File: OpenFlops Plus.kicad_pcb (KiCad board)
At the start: 2 copper layers, 111.6 x 59.4 mm, 80 parts, among them J1 Conn_02x05_Odd_Even, J2 Conn_02x05_Odd_Even, J3 Conn_01x04, P1 Conn_02x17_Odd_Even, P2 171826-4, P3 Conn_01x04, P4 Micro_SD_Card_Det1, P5 Conn_01x04, P6 Conn_01x05, Q1 BSS138, Q2 BSS138, Q3 BSS138, Q4 BSS138, Q5 BSS138, Q6 BSS138, Q7 SS8050, SW1 BT_RIGHT, SW2 BT_LEFT, U1 AMS1117-3.3, U2 STM32F105RBT6, U3 74HCT04, U4 CH213K, U5 SRV05-4, Y1 8MHz

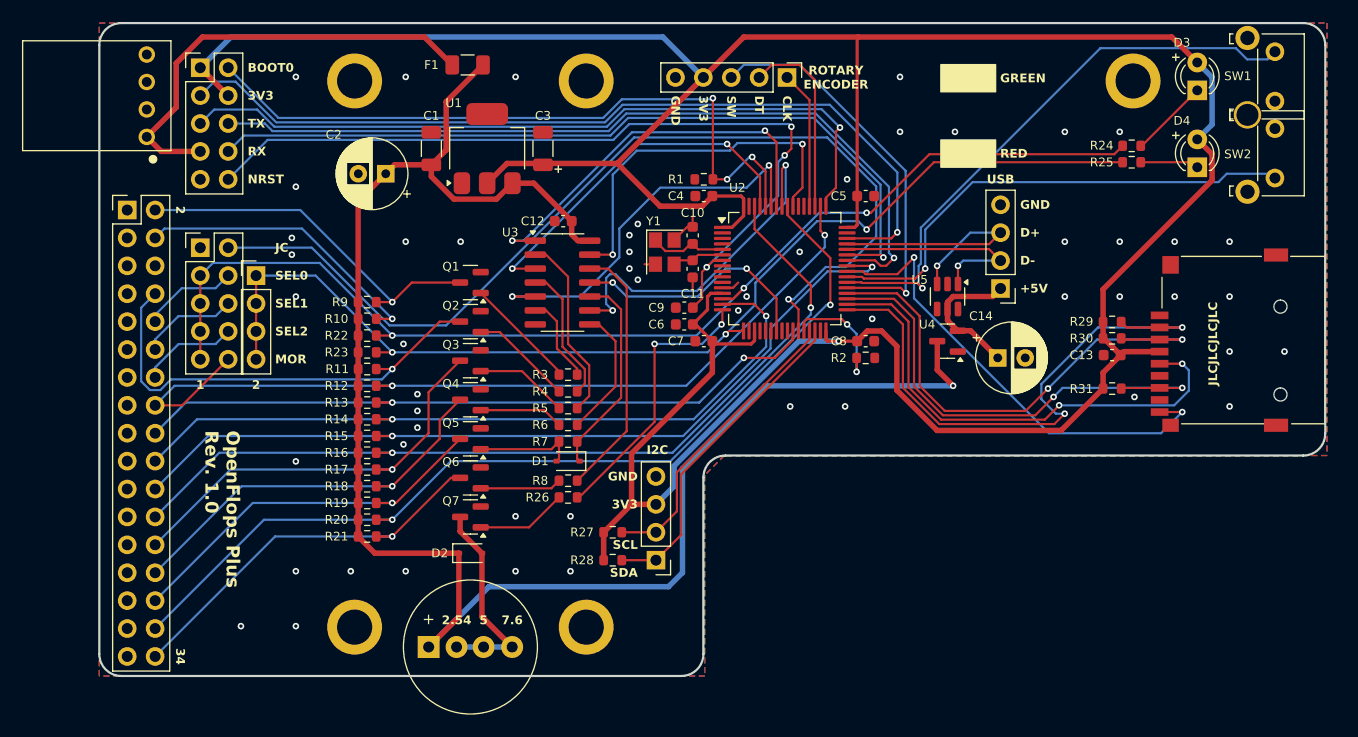
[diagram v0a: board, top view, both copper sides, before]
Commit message: Add PMOS for card reader
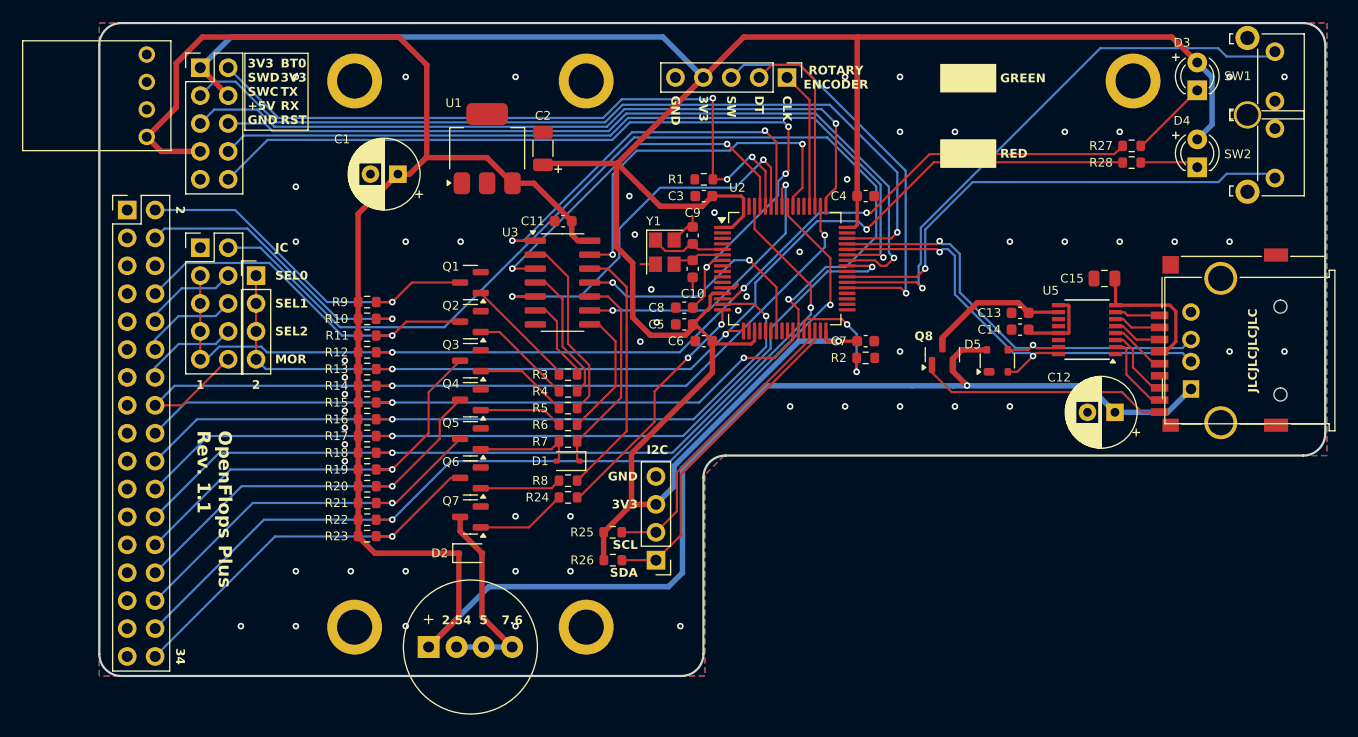
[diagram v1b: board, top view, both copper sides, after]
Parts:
- removed the C1 at (122.9, 86.7)
- removed F1: Polyfuse, Fuse:Fuse_1206_3216Metric
- removed R29, R30, R31: 47K, Resistor_SMD:R_0603_1608Metric
- removed U4: CH213K, Package_TO_SOT_SMD:SOT-23
- added C14: 4.7uF, Capacitor_SMD:C_0603_1608Metric, F.Cu at (176.5, 103.2)
- added C15: 10uF, Capacitor_SMD:C_0805_2012Metric, F.Cu at (184.2, 98.5)
- added D5: SR05, Package_TO_SOT_SMD:SOT-143, F.Cu at (174.4, 106.0)
- added Q8: AO3401A, Package_TO_SOT_SMD:SOT-23, F.Cu at (169.4, 105.5)
- C12: renamed from C13; value 10uF -> 100uF; footprint Capacitor_SMD:C_0603_1608Metric -> Capacitor_THT:CP_Radial_D6.3mm_P2.50mm
- C13: renamed from C14; value 100uF -> 1uF; footprint Capacitor_THT:CP_Radial_D6.3mm_P2.50mm -> Capacitor_SMD:C_0603_1608Metric
- P3: value Conn_01x04 -> USB_A; footprint Connector_PinHeader_2.54mm:PinHeader_1x04_P2.54mm_Vertical -> Connector_USB:USB_A_Molex_67643_Horizontal
- R25, R26: value 1K -> 4.7K
- R27, R28: value 4.7K -> 1K
- U5: value SRV05-4 -> GL823K; footprint Package_TO_SOT_SMD:SOT-23-6 -> Package_SO:SSOP-16_3.9x4.9mm_P0.635mm
- moved R24 60.5 mm to (135.4, 118.5), turned to 180 degrees
- moved R28 59.5 mm to (186.7, 88.0), turned to 0 degrees
- moved R27 58.9 mm to (186.7, 86.5), turned to 0 degrees
- moved R25 58.0 mm to (139.4, 121.6), turned to 180 degrees
- moved P3 19.6 mm to (192.1, 108.6), turned to 90 degrees
- moved R22 16.8 mm to (117.1, 120.5), turned to 0 degrees
- moved R23 16.7 mm to (117.1, 122.0), turned to 0 degrees
- moved U5 13.1 mm to (182.6, 103.2), turned to 180 degrees
- moved R26 7.02 mm to (139.4, 124.2)
- moved C12 5.21 mm to (185.2, 110.7), turned to 180 degrees
- moved C13 4.57 mm to (176.5, 101.7)
- moved R11 3.05 mm to (117.1, 103.7)
- moved R12 3.05 mm to (117.1, 105.3), turned to 180 degrees
- moved R15 3.05 mm to (117.1, 109.8)
- moved R16 3.05 mm to (117.1, 111.3)
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- renumbered C2 to C1, C11 to C10, C12 to C11, C3 to C2, C4 to C3, C5 to C4, C6 to C5, C7 to C6, C8 to C7, C9 to C8, C10 to C9
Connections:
- C12 pad 1: GND -> +5V
- C12 pad 2: +3V3 -> GND
- C13 pad 1: Net-(P3-Pin_1) -> GND
- C13 pad 2: GND -> Net-(Q8-D)
- J1 pad 7: /VBUS -> +5V
- P2 pad 1: /VBUS -> +5V
- P3 pad 1: Net-(P3-Pin_1) -> +5V
- P4 pad 1: unconnected-(P4-DAT2-Pad1) -> Net-(P4-DAT2)
- P4 pad 11: (no net) -> GND
- P4 pad 12: (no net) -> GND
- P4 pad 13: (no net) -> GND
- P4 pad 2: /SPI_NSS -> Net-(P4-DAT3/CD)
- P4 pad 3: /SPI_MOSI -> Net-(P4-CMD)
- P4 pad 4: +3V3 -> Net-(P4-VDD)
- P4 pad 5: /SPI_SCLK -> Net-(P4-CLK)
- P4 pad 7: /SPI_MISO -> Net-(P4-DAT0)
- P4 pad 8: unconnected-(P4-DAT1-Pad8) -> Net-(P4-DAT1)
- P4 pad 9: /~{SD_CD} -> /SD_DET
- R12 pad 1: +5V -> /~{SELX}
- R12 pad 2: /~{MTRON} -> +5V
- R13 pad 1: +5V -> /~{SELY}
- R13 pad 2: /~{DIR} -> +5V
- R14 pad 2: /~{STEP} -> /~{MTRON}
- R15 pad 2: /~{WDATA} -> /~{DIR}
- R16 pad 2: /~{WGATE} -> /~{STEP}
- R17 pad 2: /~{TRK0} -> /~{WDATA}
- R18 pad 2: /~{WPROT} -> /~{WGATE}
- R19 pad 2: /~{RDATA} -> /~{TRK0}
- R20 pad 2: /~{SIDE} -> /~{WPROT}
- R21 pad 2: /~{RDY} -> /~{RDATA}
- R22 pad 1: /~{SELX} -> +5V
- R22 pad 2: +5V -> /~{SIDE}
- R23 pad 1: /~{SELY} -> +5V
- R23 pad 2: +5V -> /~{RDY}
- R24 pad 1: /~{SELX} -> /SPK
- R24 pad 2: Net-(D3-K) -> Net-(Q7-B)
- R25 pad 1: /~{SELY} -> /I2C_SCL
- R25 pad 2: Net-(D4-K) -> +3V3
- R26 pad 1: /SPK -> /I2C_SDA
- R26 pad 2: Net-(Q7-B) -> +3V3
- R27 pad 1: /I2C_SCL -> /~{SELX}
- R27 pad 2: +3V3 -> Net-(D3-K)
- R28 pad 1: /I2C_SDA -> /~{SELY}
- R28 pad 2: +3V3 -> Net-(D4-K)
- U2 pad 53: unconnected-(U2-PC12-Pad53) -> GND
- U5 pad 1: /USB_D- -> GND
- U5 pad 2: GND -> Net-(P4-DAT1)
- U5 pad 3: /USB_D+ -> Net-(P4-DAT0)
- U5 pad 4: unconnected-(U5-IO3-Pad4) -> Net-(P4-CLK)
- U5 pad 5: Net-(P3-Pin_1) -> Net-(P4-CMD)
- U5 pad 6: unconnected-(U5-IO4-Pad6) -> Net-(P4-DAT3/CD)
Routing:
- net +5V: track 156.7 -> 215.5 mm
- net /SPI_NSS: track 52.7 -> 0.00 mm, vias 2 -> 0
- net +3V3: track 295.5 -> 248.2 mm
- net /SPI_MOSI: track 47.0 -> 0.00 mm, vias 2 -> 0
- net /SPI_MISO: track 45.4 -> 0.00 mm, vias 2 -> 0
- net /SPI_SCLK: track 44.8 -> 0.00 mm, vias 2 -> 0
- net /~{SD_CD}: track 42.9 -> 0.00 mm, vias 2 -> 0
- net /VBUS: track 40.4 -> 0.00 mm
- net /USB_D-: track 20.1 -> 43.4 mm, vias 1 -> 2
- net /SD_DET: track 0.00 -> 22.9 mm
- net /USB_D+: track 23.1 -> 43.1 mm, vias 1 -> 2
- net Net-(P3-Pin_1): track 13.0 -> 0.00 mm
- net Net-(Q8-D): track 0.00 -> 12.9 mm
- net Net-(P4-VDD): track 0.00 -> 12.8 mm
- net /~{INDEX}: track 42.4 -> 34.2 mm
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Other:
- board text added: "3V3 SWD SWC +5V GND"
- board text added: "BT0 3V3 TX RX RST"
- board text added: "OpenFlops Plus Rev. 1.1"
- board text removed: "+5V"
- board text removed: "BOOT0"
- board text removed: "D+"
- board text removed: "D-"
- board text removed: "NRST"
- board text removed: "OpenFlops Plus Rev. 1.0"
- board text removed: "RX"
- board text removed: "TX"
- board text removed: "USB"

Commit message: Move to 74LS07
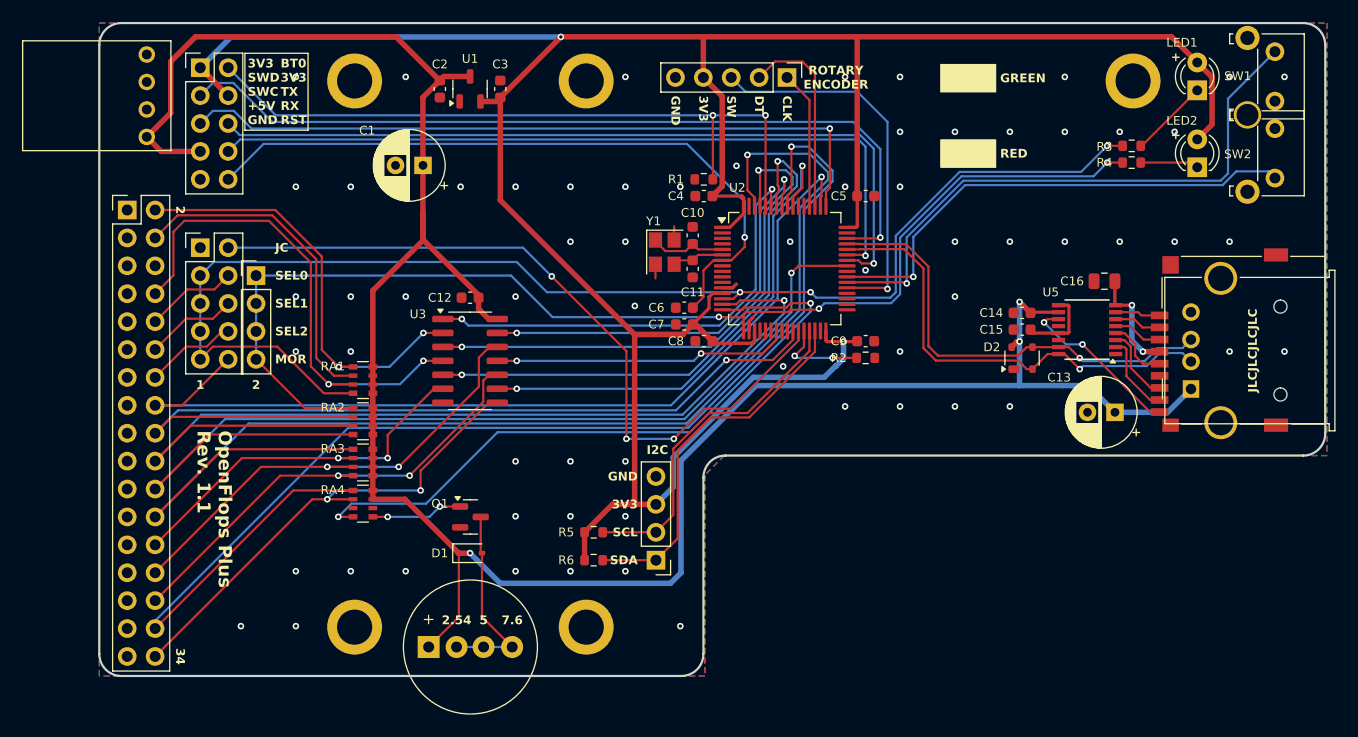
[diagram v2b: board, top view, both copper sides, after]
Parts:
- removed the C11 at (134.9, 93.3)
- removed the D1 at (135.4, 115.2)
- removed D5: SR05, Package_TO_SOT_SMD:SOT-143
- removed the Q1 at (126.5, 98.9)
- removed Q2, Q3, Q4, Q5, Q6: BSS138, Package_TO_SOT_SMD:SOT-23
- removed Q8: AO3401A, Package_TO_SOT_SMD:SOT-23
- removed R10, R11, R12, R13, R14, R15, R16, R17, R18, R19, R20, R21, R22, R23, R24, R7, R8, R9: 1K, Resistor_SMD:R_0603_1608Metric
- removed the R3 at (135.4, 107.3)
- removed the R4 at (135.4, 108.8)
- removed the R5 at (135.4, 110.3)
- removed the R6 at (135.4, 111.9)
- added C12: 100nF, Capacitor_SMD:C_0603_1608Metric, F.Cu at (126.5, 100.3)
- added C3: 1uF, Capacitor_SMD:C_0603_1608Metric, F.Cu at (129.2, 81.3)
- added D2: SR05, Package_TO_SOT_SMD:SOT-143, F.Cu at (176.7, 105.8)
- added RA1: 1K, Resistor_SMD:R_Array_Convex_4x0603, F.Cu at (116.7, 107.8)
- added RA2: 1K, Resistor_SMD:R_Array_Convex_4x0603, F.Cu at (116.7, 111.5)
- added RA3: 1K, Resistor_SMD:R_Array_Convex_4x0603, F.Cu at (116.7, 115.3)
- added RA4: 1K, Resistor_SMD:R_Array_Convex_4x0603, F.Cu at (116.7, 119.0)
- C2: value 22uF -> 1uF; footprint Capacitor_SMD:C_1206_3216Metric -> Capacitor_SMD:C_0603_1608Metric
- U1: value AMS1117-3.3 -> XC6206P332MR-G; footprint Package_TO_SOT_SMD:SOT-223-3_TabPin2 -> Package_TO_SOT_SMD:SOT-23-3
- U3: value 74HCT04 -> 74LS07
- moved U3 11.0 mm to (126.5, 106.0)
- moved C2 10.8 mm to (123.7, 81.3), turned to -90 degrees
- moved U1 5.65 mm to (126.5, 81.3)
- moved C1 2.42 mm to (122.2, 88.2)
- moved R6 1.75 mm to (137.7, 124.2)
- moved R5 1.74 mm to (137.7, 121.6)
- moved C16 0.25 mm to (184.2, 98.8)
- moved C14 0.18 mm to (176.7, 101.7)
- moved C15 0.18 mm to (176.7, 103.2)
- turned Q1 to 0 degrees
- renumbered C9 to C10, C10 to C11, C12 to C13, C13 to C14, C14 to C15, C15 to C16, C3 to C4, C4 to C5, C8 to C6, C5 to C7, C6 to C8, C7 to C9, D2 to D1, D3 to LED1, D4 to LED2, Q7 to Q1, R27 to R3, R28 to R4, R25 to R5, R26 to R6, LS1 to SPK1
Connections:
- C14 pad 2: Net-(Q8-D) -> +5V
- C2 pad 1: +3V3 -> +5V
- P4 pad 9: /SD_DET -> Net-(P4-DET)
- U3 pad 1: /~{TRK0_3V3} -> /~{DSKCHG_3V3}
- U3 pad 10: Net-(D1-K) -> /~{RDATA}
- U3 pad 12: Net-(R8-Pad1) -> /~{WPROT}
- U3 pad 13: /~{RDY_3V3} -> /~{WPROT_3V3}
- U3 pad 2: Net-(R5-Pad1) -> /~{DSKCHG}
- U3 pad 4: Net-(R4-Pad1) -> /~{INDEX}
- U3 pad 5: /~{DSKCHG_3V3} -> /~{TRK0_3V3}
- U3 pad 6: Net-(R3-Pad1) -> /~{TRK0}
- U3 pad 8: Net-(R6-Pad1) -> /~{RDY}
- U3 pad 9: /~{WPROT_3V3} -> /~{RDY_3V3}
- U5 pad 10: Net-(Q8-D) -> +5V
- U5 pad 11: unconnected-(U5-GPIO-Pad11) -> Net-(P4-DET)
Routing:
- net /SPK: track 22.7 -> 61.1 mm
- net /~{SIDE}: track 85.7 -> 118.8 mm, vias 2 -> 1
- net /~{WGATE}: track 80.8 -> 113.7 mm, vias 2 -> 1
- net Net-(R8-Pad1): track 23.5 -> 0.00 mm
- net /SD_DET: track 22.9 -> 0.00 mm
- net /JC: track 89.2 -> 68.4 mm, vias 1 -> 3
- net /~{STEP}: track 68.7 -> 89.1 mm, vias 2 -> 1
- net Net-(D1-K): track 18.9 -> 0.00 mm
- net /~{DIR}: track 63.9 -> 81.0 mm, vias 2 -> 1
- net Net-(R5-Pad1): track 17.0 -> 0.00 mm
- net /~{INDEX_3V3}: track 33.3 -> 49.6 mm
- net /~{SELX}: track 103.9 -> 120.2 mm
- net Net-(P4-DET): track 0.00 -> 15.3 mm, vias 0 -> 2
- net /~{WDATA}: track 78.5 -> 93.6 mm, vias 2 -> 1
- net /~{TRK0_3V3}: track 36.6 -> 51.1 mm
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
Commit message: Use SPI to manipulate SD card
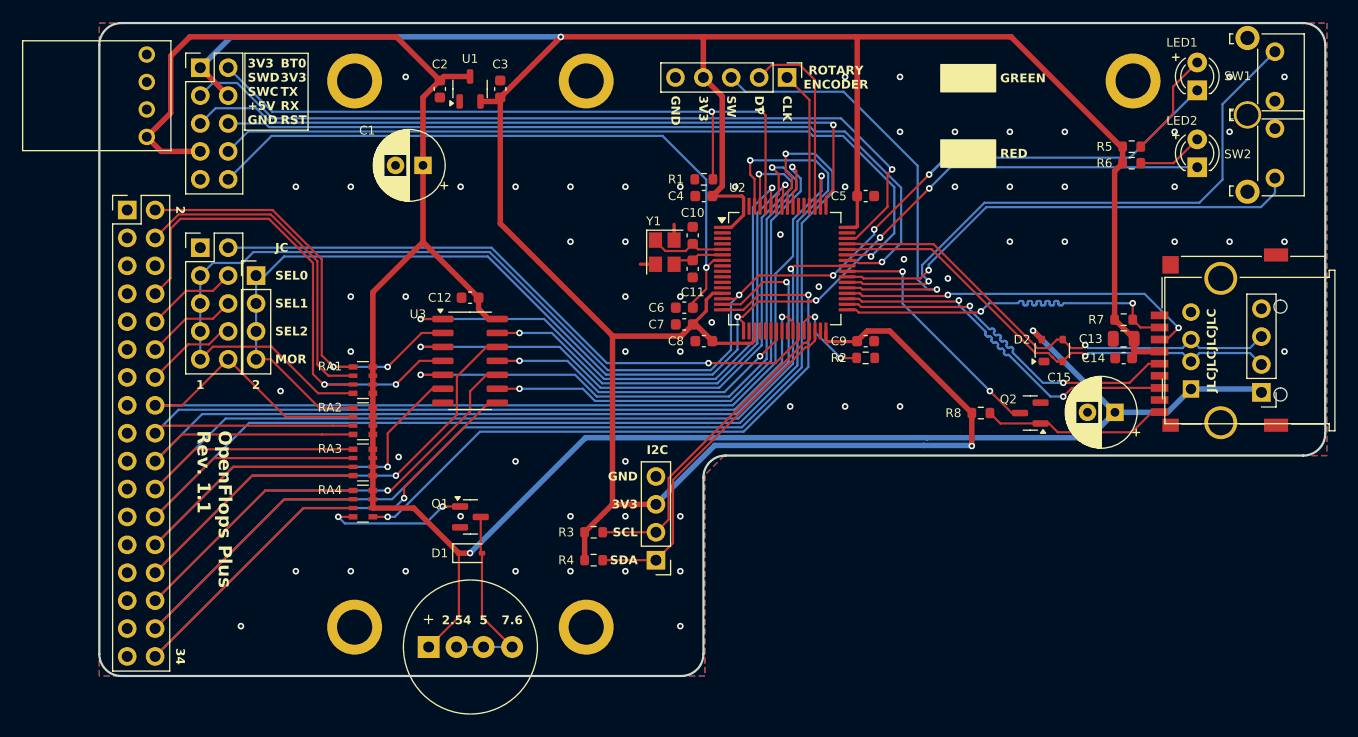
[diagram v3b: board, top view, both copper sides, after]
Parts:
- removed the C15 at (176.7, 103.2)
- removed C16: 10uF, Capacitor_SMD:C_0805_2012Metric
- removed U5: GL823K, Package_SO:SSOP-16_3.9x4.9mm_P0.635mm
- added C13: 10uF, Capacitor_SMD:C_0805_2012Metric, F.Cu at (185.9, 104.0)
- added J4: Conn_01x04, Connector_PinHeader_2.54mm:PinHeader_1x04_P2.54mm_Vertical, F.Cu at (198.5, 108.9)
- added Q2: BSS138, Package_TO_SOT_SMD:SOT-23, F.Cu at (177.4, 110.8)
- added R7: 47K, Resistor_SMD:R_0603_1608Metric, F.Cu at (185.9, 102.3)
- added R8: 10K, Resistor_SMD:R_0603_1608Metric, F.Cu at (172.9, 110.8)
- C14: value 1uF -> 100nF
- U1: value XC6206P332MR-G -> ME6211A33M3G-N
- moved C14 10.1 mm to (185.9, 105.8), turned to 180 degrees
- moved D2 2.83 mm to (179.4, 105.1)
- moved R5 0.07 mm to (186.7, 86.5), turned to 180 degrees
- turned R6 to 180 degrees
- renumbered C13 to C15, R5 to R3, R6 to R4, R3 to R5, R4 to R6
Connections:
- C14 pad 1: GND -> +3V3
- C14 pad 2: +5V -> GND
- LED1 pad 1: Net-(LED1-K) -> /~{SELX}
- LED1 pad 2: +3V3 -> Net-(LED1-A)
- LED2 pad 1: Net-(LED2-K) -> /~{SELY}
- LED2 pad 2: +3V3 -> Net-(LED2-A)
- P4 pad 1: Net-(P4-DAT2) -> unconnected-(P4-DAT2-Pad1)
- P4 pad 2: Net-(P4-DAT3/CD) -> /SPI_NSS
- P4 pad 3: Net-(P4-CMD) -> /SPI_MOSI
- P4 pad 4: Net-(P4-VDD) -> +3V3
- P4 pad 5: Net-(P4-CLK) -> /SPI_SCLK
- P4 pad 7: Net-(P4-DAT0) -> /SPI_MISO
- P4 pad 8: Net-(P4-DAT1) -> unconnected-(P4-DAT1-Pad8)
- P4 pad 9: Net-(P4-DET) -> /~{SD_CD}
- R5 pad 1: /~{SELX} -> Net-(LED1-A)
- R5 pad 2: Net-(LED1-K) -> +3V3
- R6 pad 1: /~{SELY} -> Net-(LED2-A)
- R6 pad 2: Net-(LED2-K) -> +3V3
- RA2 pad 2: /~{DIR} -> /~{MTRON}
- RA2 pad 3: /~{STEP} -> /~{DIR}
- RA2 pad 4: /~{WDATA} -> /~{STEP}
- RA3 pad 1: /~{WGATE} -> /~{WDATA}
- RA3 pad 2: /~{TRK0} -> /~{WGATE}
- RA3 pad 3: /~{WPROT} -> /~{TRK0}
- RA3 pad 4: /~{RDATA} -> /~{WPROT}
- RA4 pad 1: /~{SIDE} -> /~{RDATA}
- RA4 pad 2: /~{RDY} -> /~{SIDE}
- RA4 pad 3: (no net) -> /~{RDY}
- RA4 pad 4: /SPK -> Net-(Q1-B)
- RA4 pad 5: Net-(Q1-B) -> /SPK
- RA4 pad 6: (no net) -> +5V
- U2 pad 40: /~{SD_CD} -> /SD_CD
- U2 pad 53: GND -> unconnected-(U2-PC12-Pad53)
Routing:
- net +3V3: track 254.1 -> 288.7 mm
- net /SPI_MOSI: track 0.00 -> 33.8 mm, vias 0 -> 2
- net /SPI_MISO: track 0.00 -> 33.7 mm, vias 0 -> 2
- net /SPI_NSS: track 0.00 -> 33.7 mm, vias 0 -> 2
- net /SPI_SCLK: track 0.00 -> 33.6 mm, vias 0 -> 2
- net /SD_CD: track 0.00 -> 22.8 mm, vias 0 -> 2
- net /~{RDY}: track 44.1 -> 65.0 mm, vias 2 -> 1
- net /~{RDATA}: track 42.2 -> 63.0 mm, vias 2 -> 1
- net /~{TRK0}: track 34.7 -> 54.8 mm, vias 2 -> 1
- net /~{WPROT}: track 43.6 -> 63.4 mm, vias 2 -> 1
- net /~{MTRON}: track 84.5 -> 101.6 mm
- net /~{SD_CD}: track 0.00 -> 16.9 mm
- net /~{SELX}: track 120.2 -> 137.0 mm, vias 3 -> 4
- net Net-(P4-DET): track 15.3 -> 0.00 mm, vias 2 -> 0
- net /~{SELY}: track 109.0 -> 120.2 mm, vias 3 -> 4
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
